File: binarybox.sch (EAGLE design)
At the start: 39 parts, among them IC2 MAX7219CNG

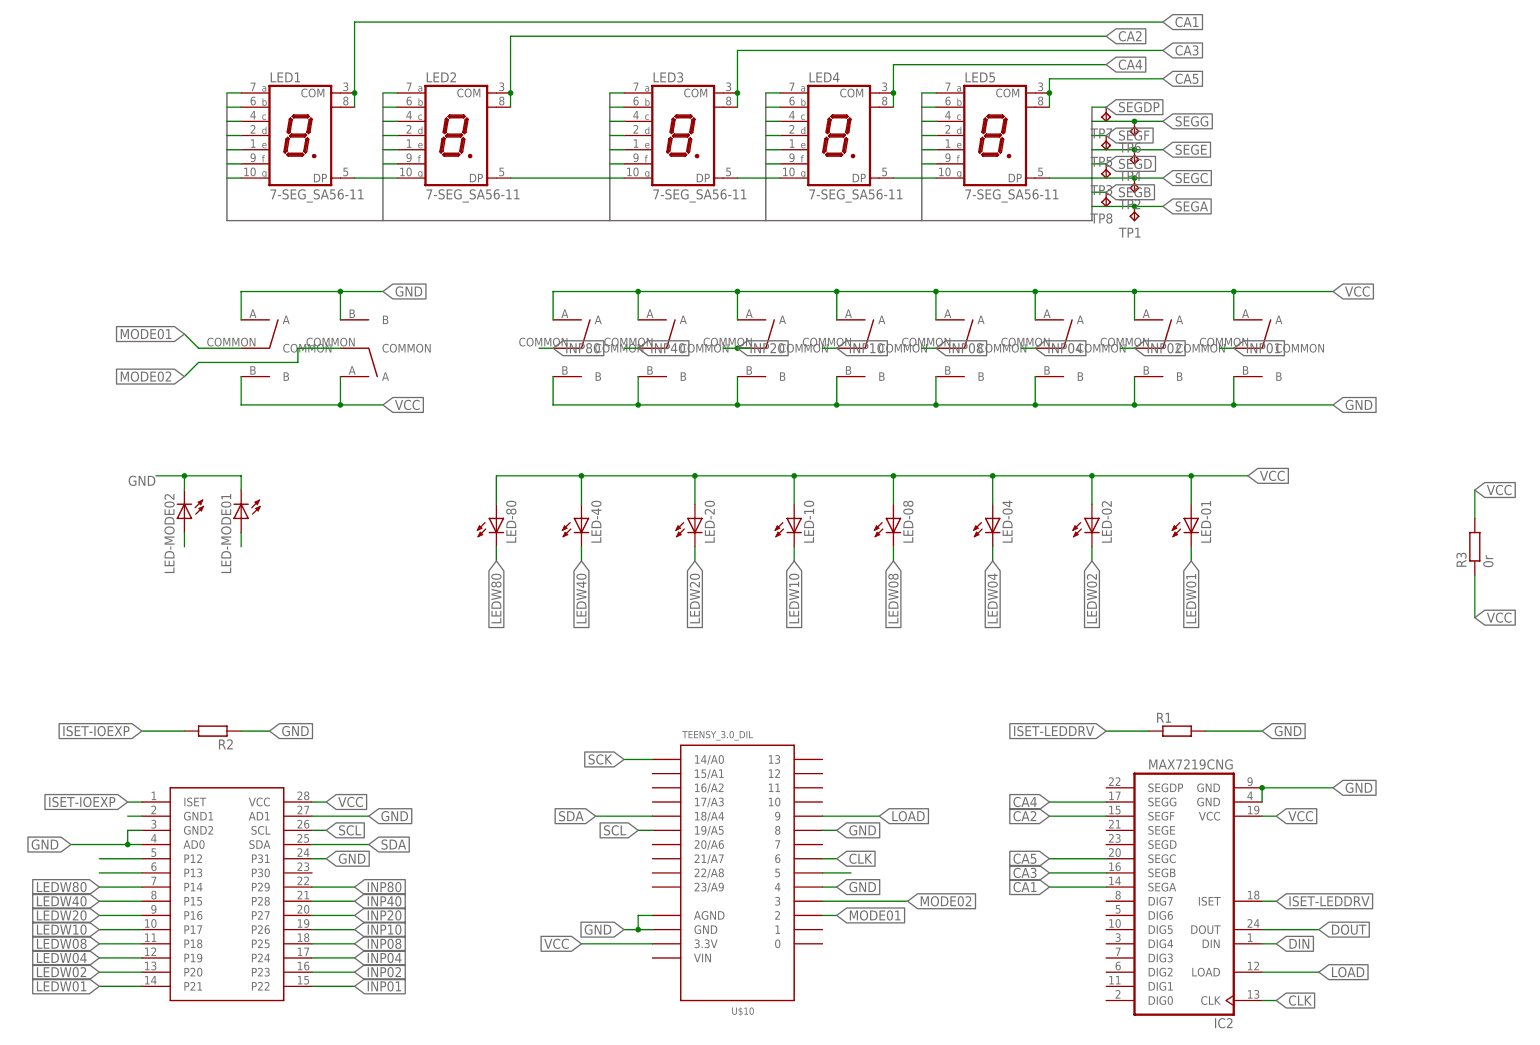
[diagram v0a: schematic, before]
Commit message: rework - removing io expander
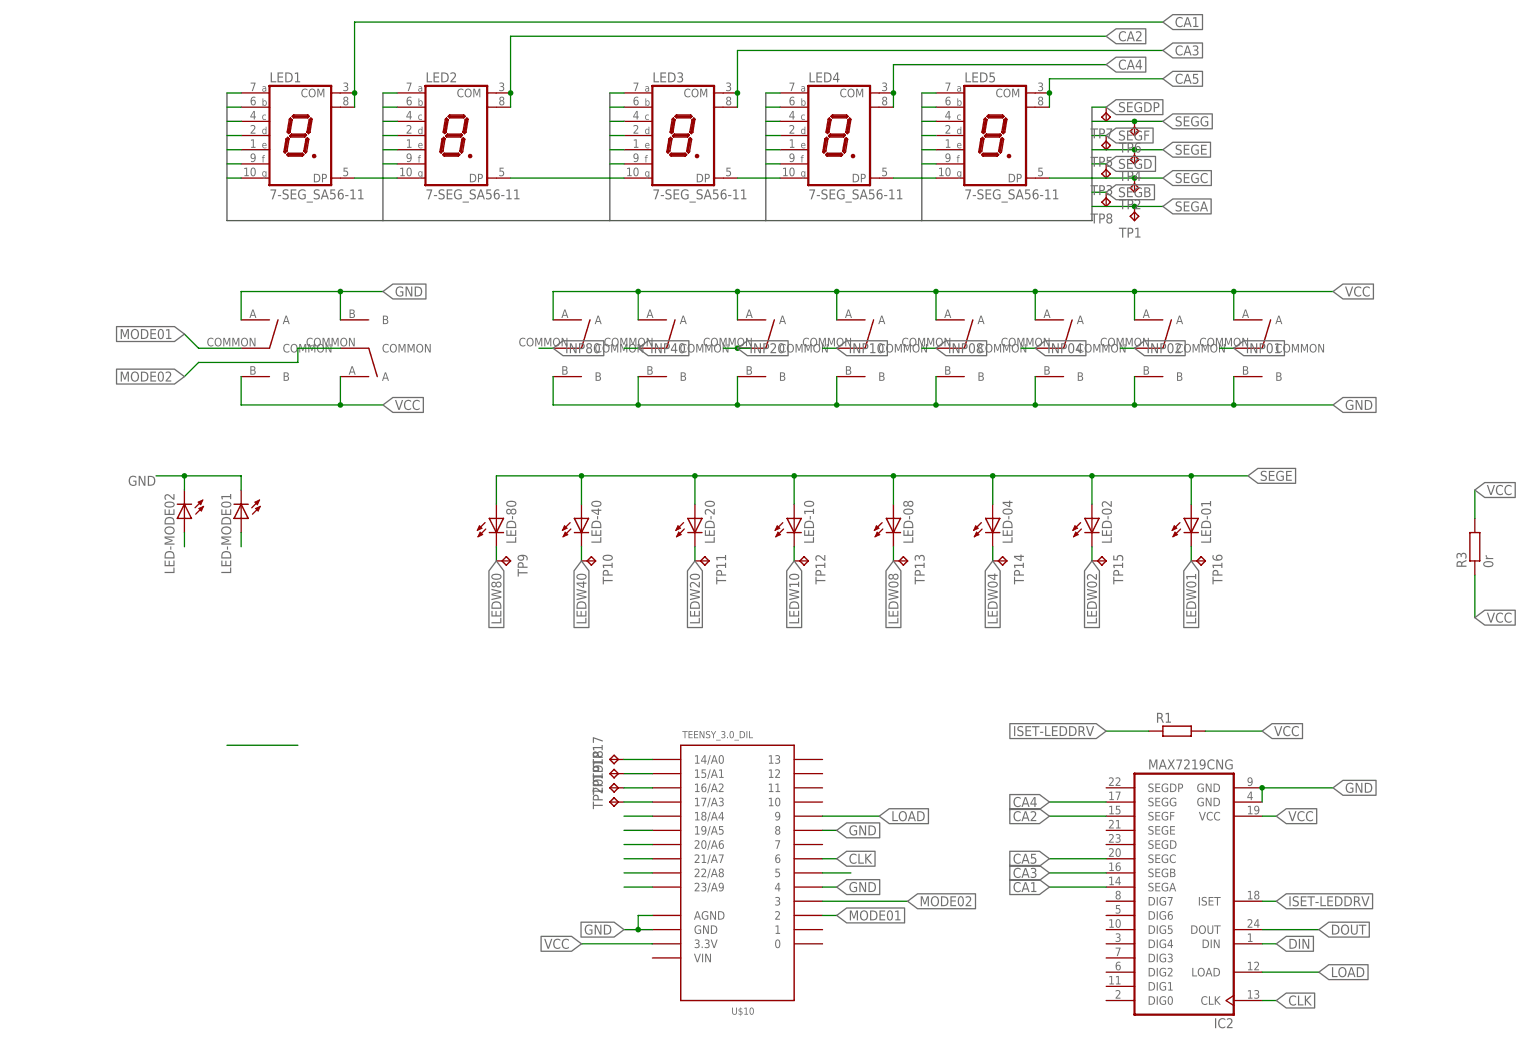
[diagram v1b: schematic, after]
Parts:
- removed R2: (no value), resistor:R-EU_0207/10
- removed U$9: MAX6956DIL28-3, max6956-special:MAX6956DIL28-3
- added TP10, TP11, TP12, TP13, TP14, TP15, TP16, TP17, TP18, TP19, TP20, TP9: TPB1,27, testpad:TPB1,27
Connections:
- removed net ISET-IOEXP: R2.2, U$9.ISET
- removed net SCK: U$10.14/A0
- removed net SCL: U$10.19/A5, U$9.SCL
- removed net SDA: U$10.18/A4, U$9.SDA
- new net N$10: TP18.TP, U$10.15/A1
- new net N$11: TP19.TP, U$10.16/A2
- new net N$12: TP20.TP, U$10.17/A3
- new net N$13: U$10.18/A4
- new net N$14: U$10.19/A5
- new net N$15: U$10.20/A6
- new net N$16: U$10.21/A7
- new net N$36: U$10.22/A8
- new net N$37: U$10.23/A9
- new net N$9: TP17.TP, U$10.14/A0
- net GND: no longer R1.2, R2.1, U$9.AD0, U$9.AD1, U$9.GND2, U$9.P31
- net INP01: no longer U$9.P22
- net INP02: no longer U$9.P23
- net INP04: no longer U$9.P24
- net INP08: no longer U$9.P25
- net INP10: no longer U$9.P26
- net INP20: no longer U$9.P27
- net INP40: no longer U$9.P28
- net INP80: no longer U$9.P29
- net LEDMODE01: no longer U$9.P13
- net LEDMODE02: no longer U$9.P12
- net LEDW01: now also TP16.TP; no longer U$9.P21
- net LEDW02: now also TP15.TP; no longer U$9.P20
- net LEDW04: now also TP14.TP; no longer U$9.P19
- net LEDW08: now also TP13.TP; no longer U$9.P18
- net LEDW10: now also TP12.TP; no longer U$9.P17
- net LEDW20: now also TP11.TP; no longer U$9.P16
- net LEDW40: now also TP10.TP; no longer U$9.P15
- net LEDW80: now also TP9.TP; no longer U$9.P14
- net SEGE: now also LED-01.A, LED-02.A, LED-04.A, LED-08.A, LED-10.A, LED-20.A, LED-40.A, LED-80.A
- net VCC: now also R1.2; no longer LED-01.A, LED-02.A, LED-04.A, LED-08.A, LED-10.A, LED-20.A, LED-40.A, LED-80.A, U$9.GND1, U$9.VCC
